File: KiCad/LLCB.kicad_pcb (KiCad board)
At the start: 2 copper layers, 51 x 64 mm, 18 parts, among them J1 Conn_02x24_Odd_Even, J2 Conn_01x24, J3 Conn_02x24_Odd_Even, J4 Conn_01x24, J5 Barrel_Jack_Switch, J6 Conn_02x01, J7 Conn_02x06_Odd_Even, J8 Conn_02x06_Odd_Even, J9 Conn_02x02_Odd_Even, SW1 SW_Push_DPDT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

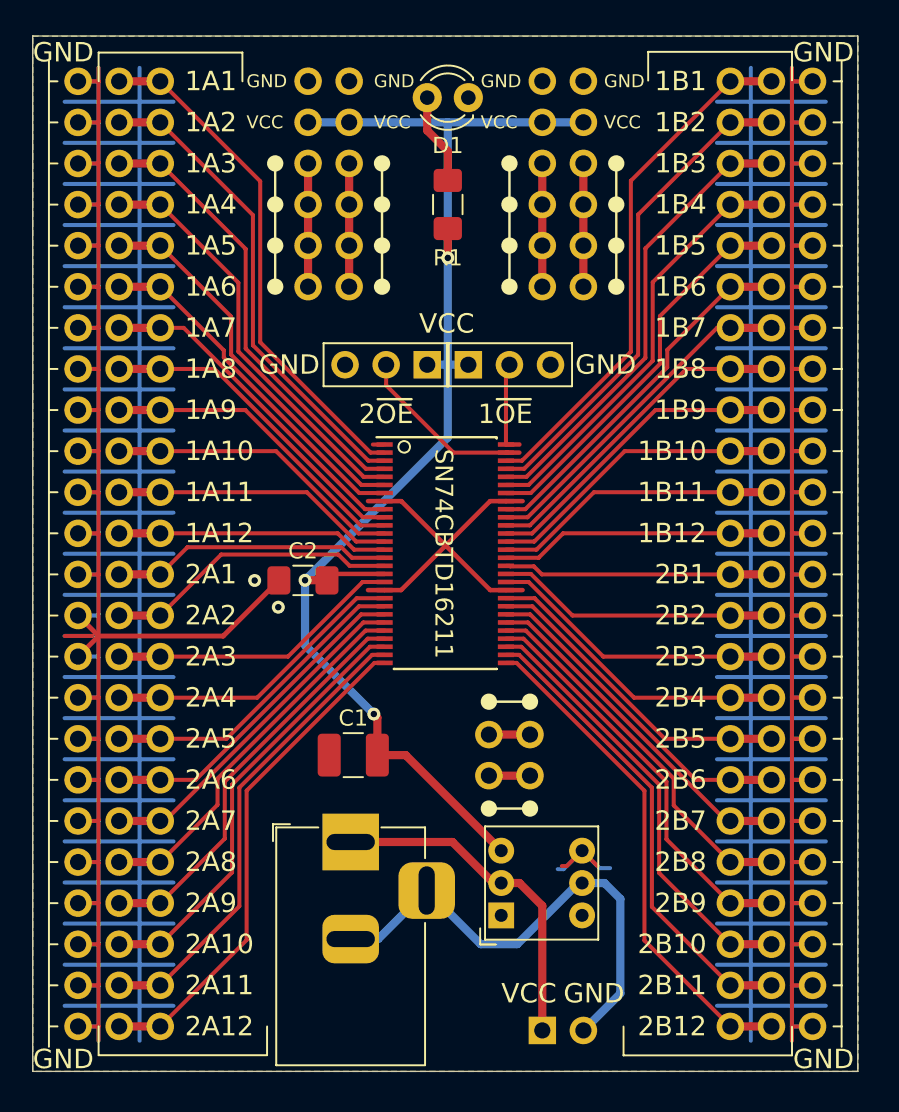
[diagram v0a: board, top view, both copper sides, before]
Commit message: Created SSOP variant of board
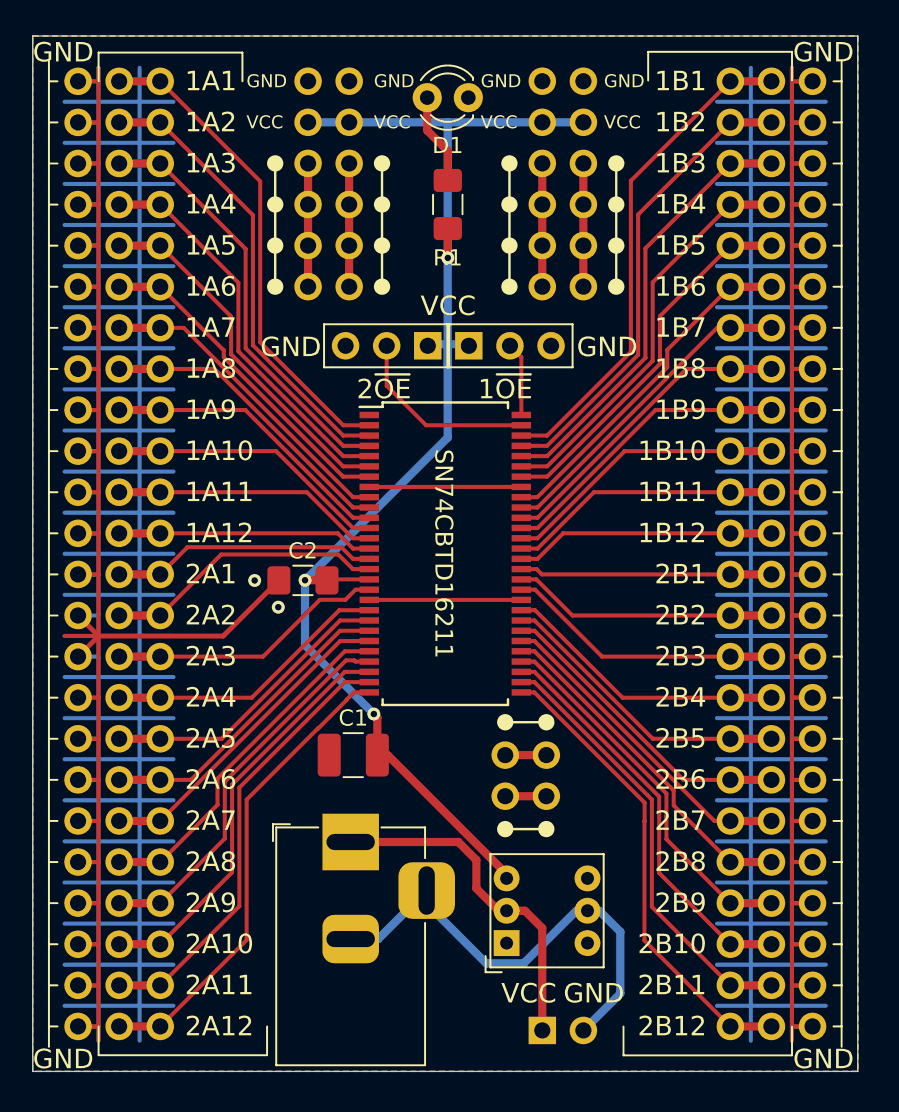
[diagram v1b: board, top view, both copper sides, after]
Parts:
- removed REF**: OSHW-Logo_11.4x12mm_SilkScreen, Symbol:OSHW-Logo_11.4x12mm_SilkScreen
- U1: footprint Package_SO:TSSOP-56_6.1x14mm_P0.5mm -> Package_SO:SSOP-56_7.5x18.5mm_P0.635mm
- moved SW1 1.75 mm to (159.3, 116.1)
- moved J9 1.62 mm to (159.2, 104.5)
- moved JP2 1.17 mm to (154.4, 79.1)
- moved JP1 1.17 mm to (157.0, 79.1)
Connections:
- net /1~OE renamed /1~{OE}
- net /2~OE renamed /2~{OE}
- net GNDPWR renamed /GNDPWR
- net VIN renamed /VIN
- SW1 pad 1: Net-(SW1-Pad1) -> unconnected-(SW1-A-Pad1)
- SW1 pad 4: Net-(SW1-Pad4) -> unconnected-(SW1-A-Pad4)
- U1 pad 1: /NC -> unconnected-(U1-NC-Pad1)
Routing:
- net GND: track 839.9 -> 827.9 mm
- net 2B12: track 31.1 -> 29.0 mm
- net 2B11: track 29.2 -> 27.1 mm
- net 2B10: track 27.2 -> 25.2 mm
- net VCC: track 81.2 -> 83.2 mm
- net 2A12: track 31.1 -> 29.1 mm
- net 2B9: track 25.3 -> 23.3 mm
- net 2B8: track 23.3 -> 21.4 mm
- net 2A11: track 29.2 -> 27.5 mm
- net 1A1: track 31.7 -> 30.1 mm
- net 1B1: track 32.3 -> 30.7 mm
- net 2A10: track 27.2 -> 25.6 mm
- net 1A2: track 29.8 -> 28.2 mm
- net 1A3: track 27.8 -> 26.3 mm
- net 1B2: track 30.4 -> 28.8 mm
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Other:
- net class Default removed
- board text added: "1~{OE}"
- board text added: "2~{OE}"
- board text added: "Design by J.Bilander Modified by P.Bengtsson"
- board text removed: "1~OE"
- board text removed: "2~OE"
- board text removed: "Design by J.Bilander"
